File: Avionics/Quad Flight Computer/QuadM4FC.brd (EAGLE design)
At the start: 50.8 x 50.5 mm, 5 parts, among them U1 INF-PG-LQFP-100-11-7000X7000E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, U2 MPU-9250, U3 MPL115A2, U4 S25FL127S, U5 CC2520

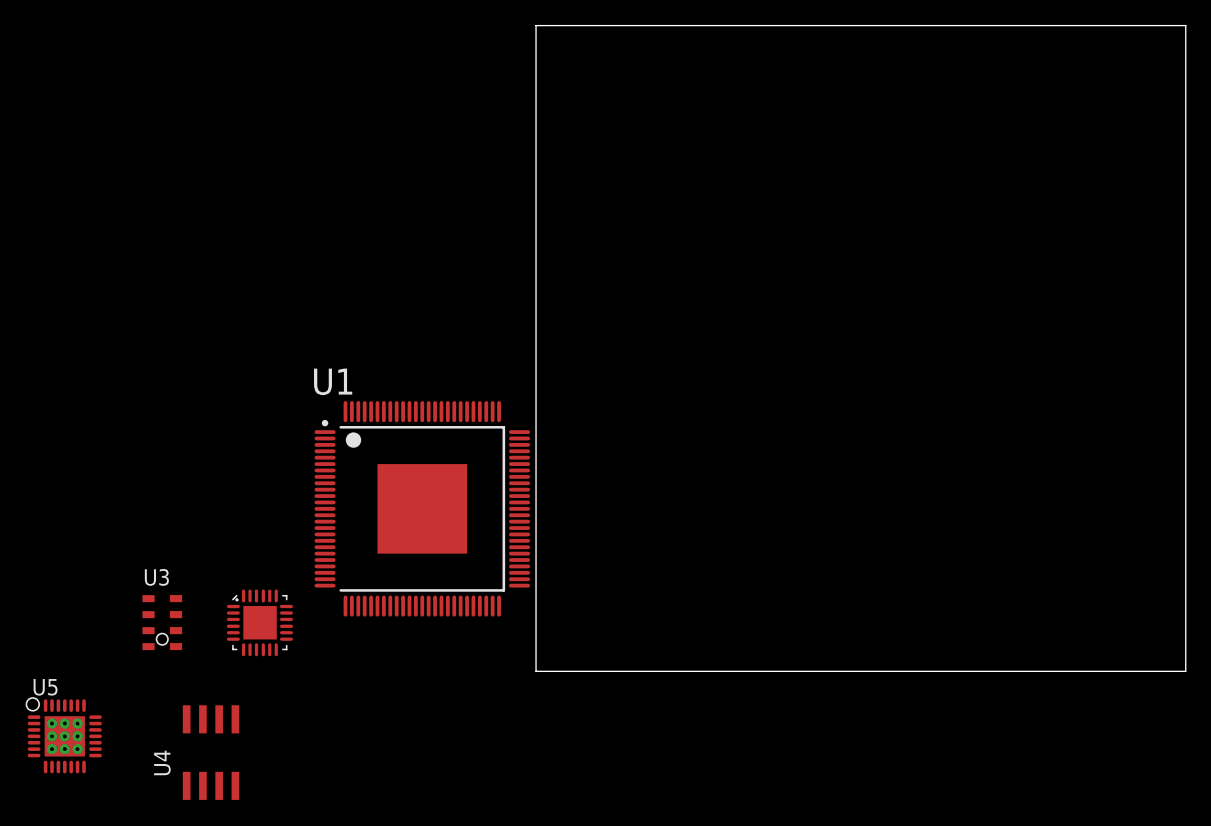
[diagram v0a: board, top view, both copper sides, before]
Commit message: Added radio components
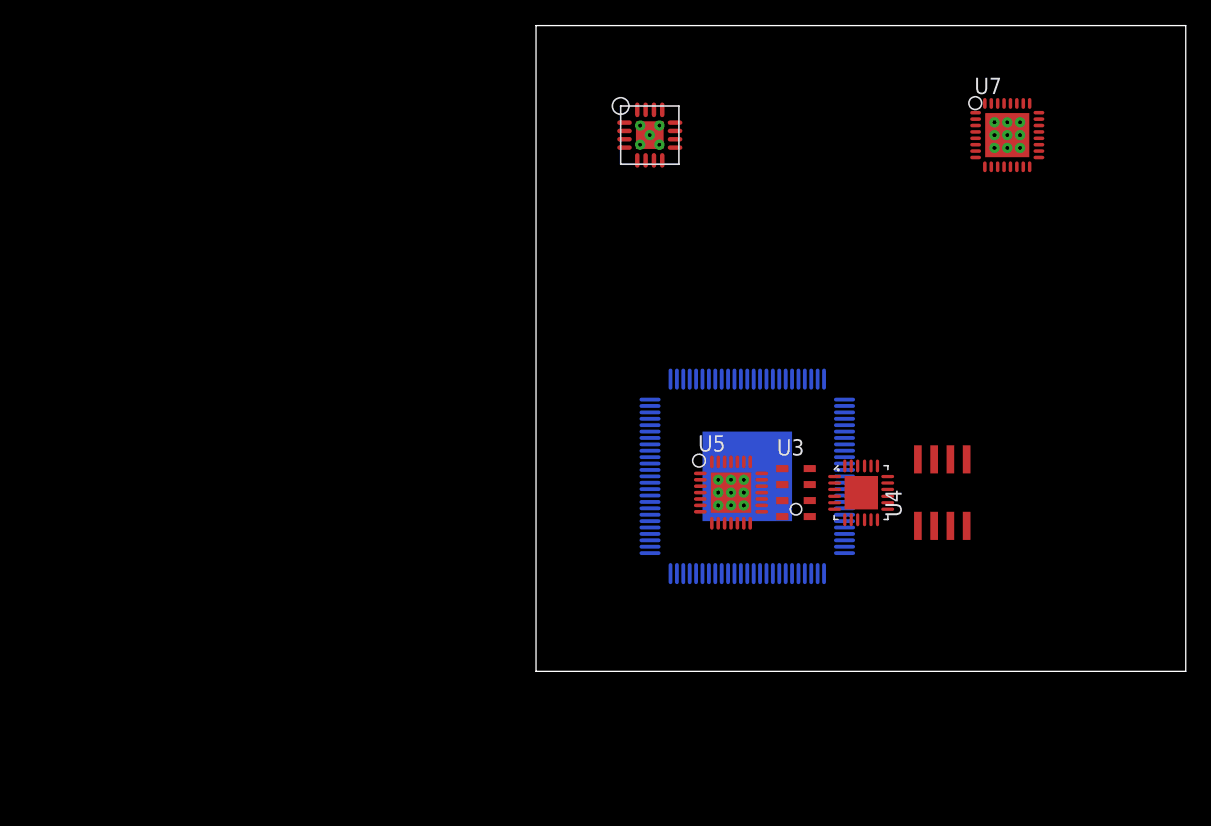
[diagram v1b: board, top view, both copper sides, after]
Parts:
- added U6: CC2592, ti_rf:RGV_S-PVGFN-N16
- added U7: CC1120, ti_rf:RHB_S-PVQFN-N32
- moved U4 60.7 mm to (31.8, 14.0)
- moved U5 55.4 mm to (15.2, 14.0)
- moved U3 50.6 mm to (20.3, 14.0)
- moved U2 48.1 mm to (25.4, 14.0)
- moved U1 25.5 mm to (16.5, 15.2), flipped to the bottom
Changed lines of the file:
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@@
 </autorouter>
 <elements>
-<element name="U1" library="XMC4500-F100K1024 AB" package="INF-PG-LQFP-100-11-7000X7000E9PRIMARY" value="INF-PG-LQFP-100-11-7000X7000E9LQFP-100" x="-8.89" y="12.7"/>
-<element name="U2" library="Invesense" package="QFN-24-4MM2" value="MPU-9250" x="-21.59" y="3.81"/>
-<element name="U3" library="Sensors" package="MPL115A2" value="MPL115A2" x="-29.21" y="3.81"/>
-<element name="U4" library="memory" package="SO8" value="S25FL127S" x="-25.4" y="-6.35"/>
-<element name="U5" library="ti_rf" package="RHD_S-PVQFN-N28" value="CC2520" x="-36.83" y="-5.08"/>
+<element name="U1" library="XMC4500-F100K1024 AB" package="INF-PG-LQFP-100-11-7000X7000E9PRIMARY" value="INF-PG-LQFP-100-11-7000X7000E9LQFP-100" x="16.51" y="15.24" rot="MR0"/>
+<element name="U2" library="Invesense" package="QFN-24-4MM2" value="MPU-9250" x="25.4" y="13.97"/>
+<element name="U3" library="Sensors" package="MPL115A2" value="MPL115A2" x="20.32" y="13.97"/>
+<element name="U4" library="memory" package="SO8" value="S25FL127S" x="31.75" y="13.97"/>
+<element name="U5" library="ti_rf" package="RHD_S-PVQFN-N28" value="CC2520" x="15.24" y="13.97"/>
+<element name="U6" library="ti_rf" package="RGV_S-PVGFN-N16" value="CC2592" x="8.89" y="41.91"/>
+<element name="U7" library="ti_rf" package="RHB_S-PVQFN-N32" value="CC1120" x="36.83" y="41.91"/>
 </elements>
 <signals>
@@
 <contactref element="U2" pad="18"/>
 <contactref element="U2" pad="EP"/>
-<wire x1="-19.5038" y1="5.0667" x2="-21.57" y2="3.8" width="0" layer="19" extent="1-1"/>
+<wire x1="27.4862" y1="15.2267" x2="25.42" y2="13.96" width="0" layer="19" extent="1-1"/>
 </signal>
 <signal name="VDD">

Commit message: Added RF base station project
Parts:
- added U8: CC1190, ti_rf:RGV_S-PVGFN-N16
- moved U5 21.3 mm to (8.89, 34.3)
- moved U7 7.62 mm to (36.8, 34.3)
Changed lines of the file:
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@@
 <element name="U3" library="Sensors" package="MPL115A2" value="MPL115A2" x="20.32" y="13.97"/>
 <element name="U4" library="memory" package="SO8" value="S25FL127S" x="31.75" y="13.97"/>
-<element name="U5" library="ti_rf" package="RHD_S-PVQFN-N28" value="CC2520" x="15.24" y="13.97"/>
+<element name="U5" library="ti_rf" package="RHD_S-PVQFN-N28" value="CC2520" x="8.89" y="34.29"/>
 <element name="U6" library="ti_rf" package="RGV_S-PVGFN-N16" value="CC2592" x="8.89" y="41.91"/>
-<element name="U7" library="ti_rf" package="RHB_S-PVQFN-N32" value="CC1120" x="36.83" y="41.91"/>
+<element name="U7" library="ti_rf" package="RHB_S-PVQFN-N32" value="CC1120" x="36.83" y="34.29"/>
+<element name="U8" library="ti_rf" package="RGV_S-PVGFN-N16" value="CC1190" x="36.83" y="43.18"/>
 </elements>
 <signals>
